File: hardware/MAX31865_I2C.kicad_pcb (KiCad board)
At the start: 2 copper layers, 25.4 x 27.9 mm, 38 parts, among them J1 Conn_01x08, J2 AVR-ISP-6, J3 Conn_02x04_Odd_Even, J4 Conn_02x04_Odd_Even, J5 Conn_02x02_Odd_Even, U1 ATmega48A-A, Y1 16MHz

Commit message: added comments for inputs / output connections
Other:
- board text added: "AVR ISP"
- board text added: "GPIO Digital In / Out Analog In depending on configuration"
- board text added: "I2C bus connection"
- board text added: "UART"
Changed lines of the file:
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@@
     (effects (font (size 1 1) (thickness 0.2) bold) (justify bottom))
+  )
+  (gr_text "GPIO\nDigital In / Out\nAnalog In\n\ndepending on configuration" (at 135.128 112.9792) (layer "Cmts.User")
+    (effects (font (size 1 1) (thickness 0.15)) (justify right bottom))
+  )
+  (gr_text "I2C bus connection" (at 166.9796 110.1852 90) (layer "Cmts.User")
+    (effects (font (size 1 1) (thickness 0.15)) (justify left bottom))
+  )
+  (gr_text "AVR ISP" (at 135.2296 103.0224 90) (layer "Cmts.User")
+    (effects (font (size 1 1) (thickness 0.15)) (justify left bottom))
+  )
+  (gr_text "UART" (at 142.1384 90.5256) (layer "Cmts.User")
+    (effects (font (size 1 1) (thickness 0.15)) (justify left bottom))
   )
   (dimension (type aligned) (layer "Dwgs.User")

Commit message: added MadeByJochen logo
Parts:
- added G***: LOGO, MadeByJochen:MadeByJochen_5x5, F.Cu at (153.2, 102.2)

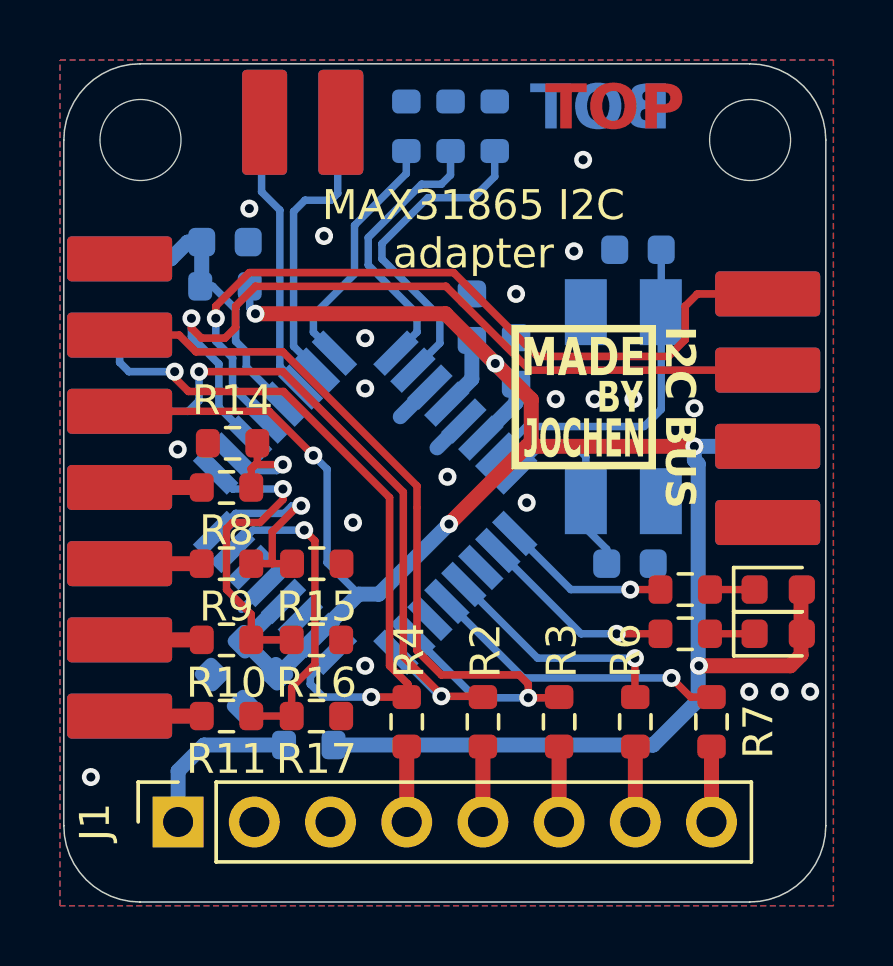
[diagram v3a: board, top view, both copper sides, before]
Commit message: added Revision Text Variable to PCB
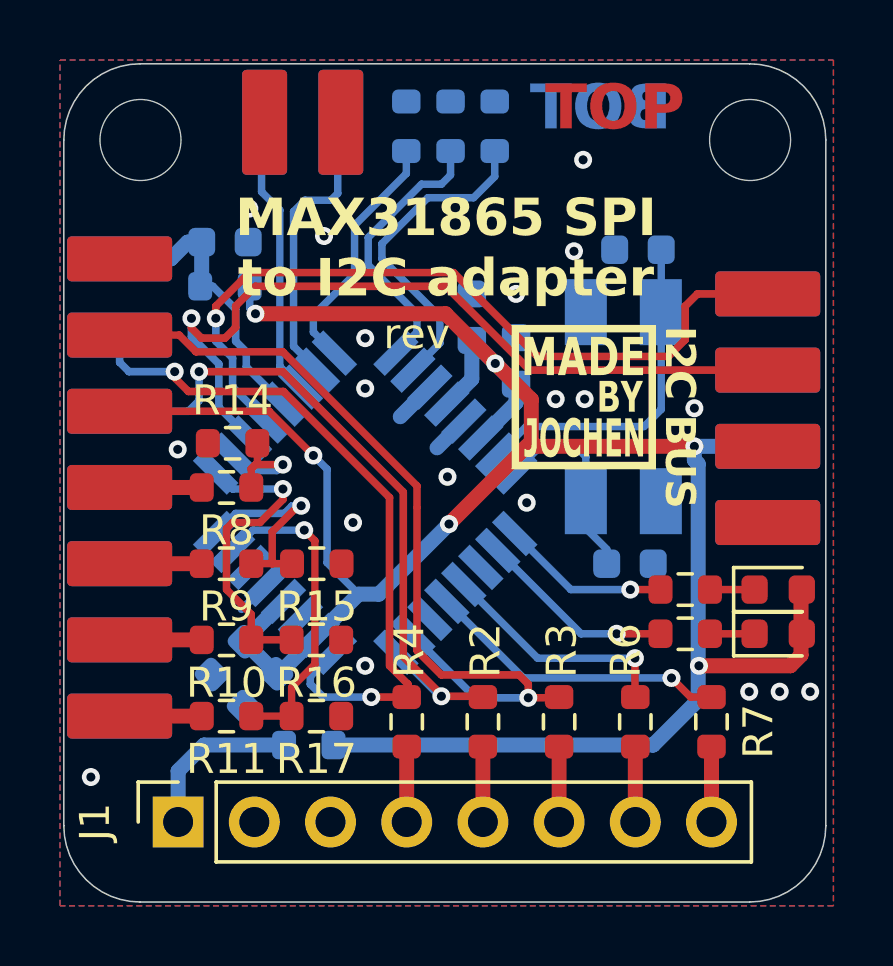
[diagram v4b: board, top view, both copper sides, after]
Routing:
- net GND: vias 20 -> 19
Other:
- board text added: "MAX31865 SPI to I2C adapter"
- board text added: "rev ${REVISION}"
- board text removed: "MAX31865 I2C adapter"
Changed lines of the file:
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@@
     )
   )
+  (property "REVISION" "1")
   (net 0 "")
   (net 1 "GND")
@@
     (effects (font (size 1 1) (thickness 0.15)) (justify left bottom mirror))
   )
-  (gr_text "MAX31865 I2C\nadapter" (at 149.4536 97.9424) (layer "F.SilkS")
-    (effects (font (size 1 1) (thickness 0.15)) (justify bottom))
+  (gr_text "MAX31865 SPI\nto I2C adapter" (at 148.5392 98.9076) (layer "F.SilkS")
+    (effects (font (size 1.25 1.25) (thickness 0.3) bold) (justify bottom))
   )
   (gr_text "I2C BUS" (at 155.7528 102.8192 270) (layer "F.SilkS")
     (effects (font (size 1 1) (thickness 0.2) bold) (justify bottom))
   )
+  (gr_text "rev ${REVISION}" (at 146.4564 100.6348) (layer "F.SilkS")
+    (effects (font (size 1 1) (thickness 0.15)) (justify left bottom))
+  )
   (gr_text "GPIO\nDigital In / Out\nAnalog In\n\ndepending on configuration" (at 135.128 112.9792) (layer "Cmts.User")
     (effects (font (size 1 1) (thickness 0.15)) (justify right bottom))
@@
   (via (at 160.6804 111.9632) (size 0.6) (drill 0.3) (layers "F.Cu" "B.Cu") (free) (net 1))
   (via (at 136.7028 114.808) (size 0.6) (drill 0.3) (layers "F.Cu" "B.Cu") (free) (net 1))
-  (via (at 154.7876 102.2096) (size 0.6) (drill 0.3) (layers "F.Cu" "B.Cu") (free) (net 1))
   (via (at 145.8468 101.854) (size 0.6) (drill 0.3) (layers "F.Cu" "B.Cu") (free) (net 1))
   (via (at 156.8196 102.5144) (size 0.6) (drill 0.3) (layers "F.Cu" "B.Cu") (free) (net 1))
   (via (at 150.876 98.7044) (size 0.6) (drill 0.3) (layers "F.Cu" "B.Cu") (free) (net 1))
   (via (at 139.5984 103.886) (size 0.6) (drill 0.3) (layers "F.Cu" "B.Cu") (free) (net 1))
-  (via (at 153.4922 102.2096) (size 0.6) (drill 0.3) (layers "F.Cu" "B.Cu") (free) (net 1))
+  (via (at 153.162 102.2096) (size 0.6) (drill 0.3) (layers "F.Cu" "B.Cu") (free) (net 1))
   (via (at 158.6484 111.9632) (size 0.6) (drill 0.3) (layers "F.Cu" "B.Cu") (free) (net 1))
   (via (at 145.8468 100.1776) (size 0.6) (drill 0.3) (layers "F.Cu" "B.Cu") (free) (net 1))

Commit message: tiny update to schematic and pcb
updated to KiCAD v7 release version
updated version in PCB
updated LED colors
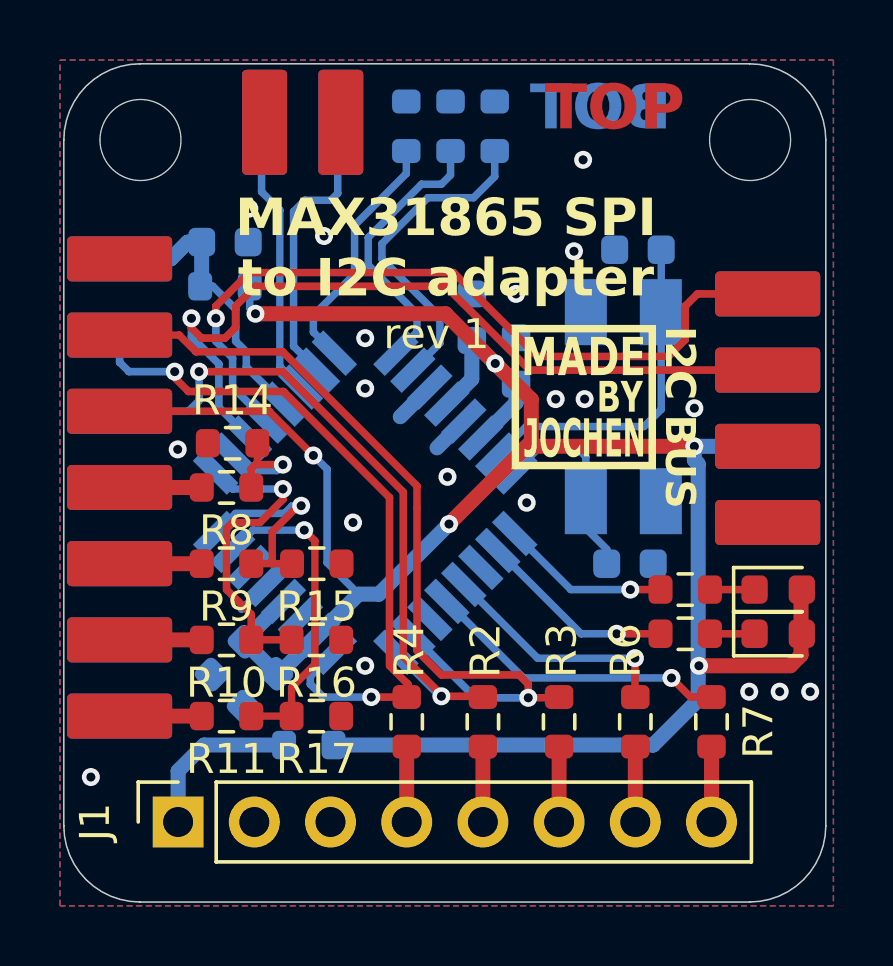
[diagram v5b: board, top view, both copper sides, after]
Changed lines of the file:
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@@
   (paper "A4")
   (title_block
+    (title "MAX31865 SPI to I2C bridge")
+    (rev "1")
     (comment 4 "AISLER Project ID: IYFKSMYY")
   )
